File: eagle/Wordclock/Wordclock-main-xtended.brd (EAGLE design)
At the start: 100 x 50 mm, 59 parts, among them IC1 MEGA8-P, J1 AVR_SPI_PRG_6PTH, Q1 16MHz, T1 EBC pinout

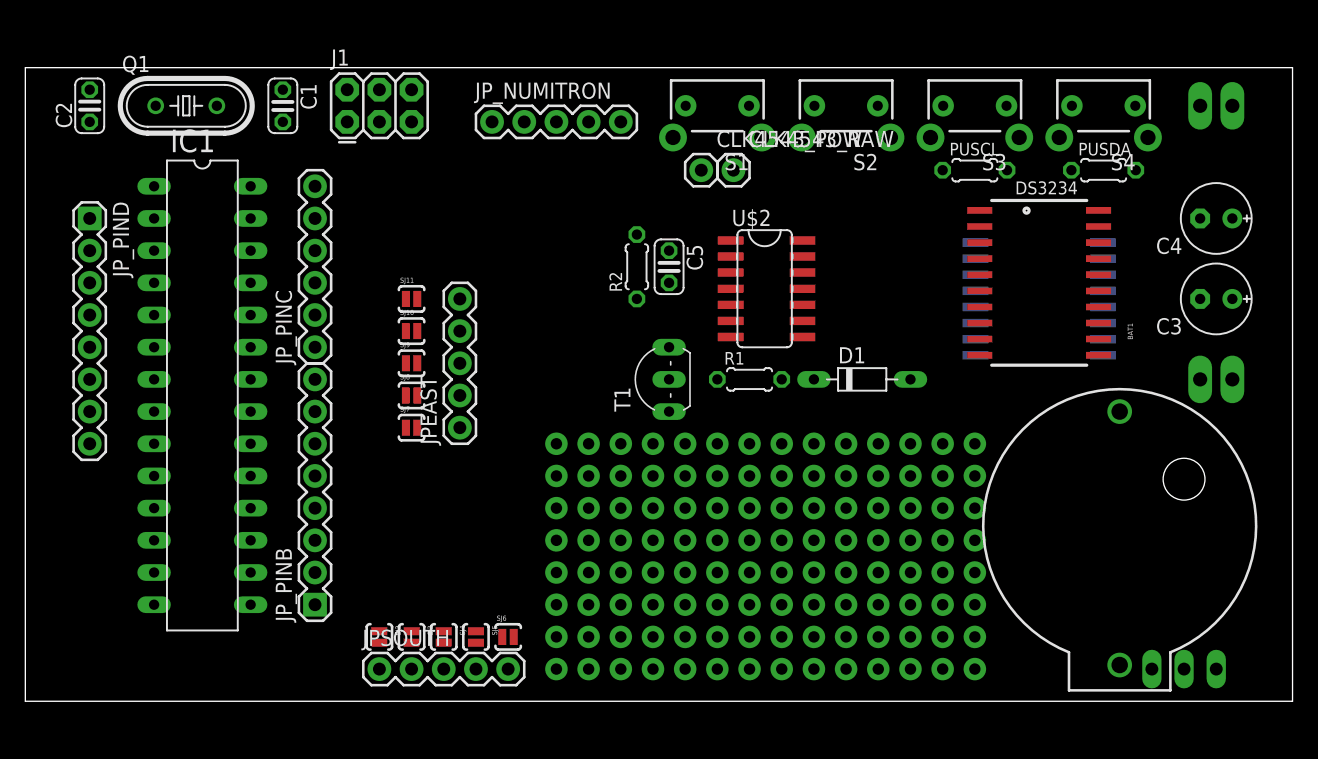
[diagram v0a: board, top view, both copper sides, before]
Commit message: Worclock extended version wired beta, wired. Todo verify before production.
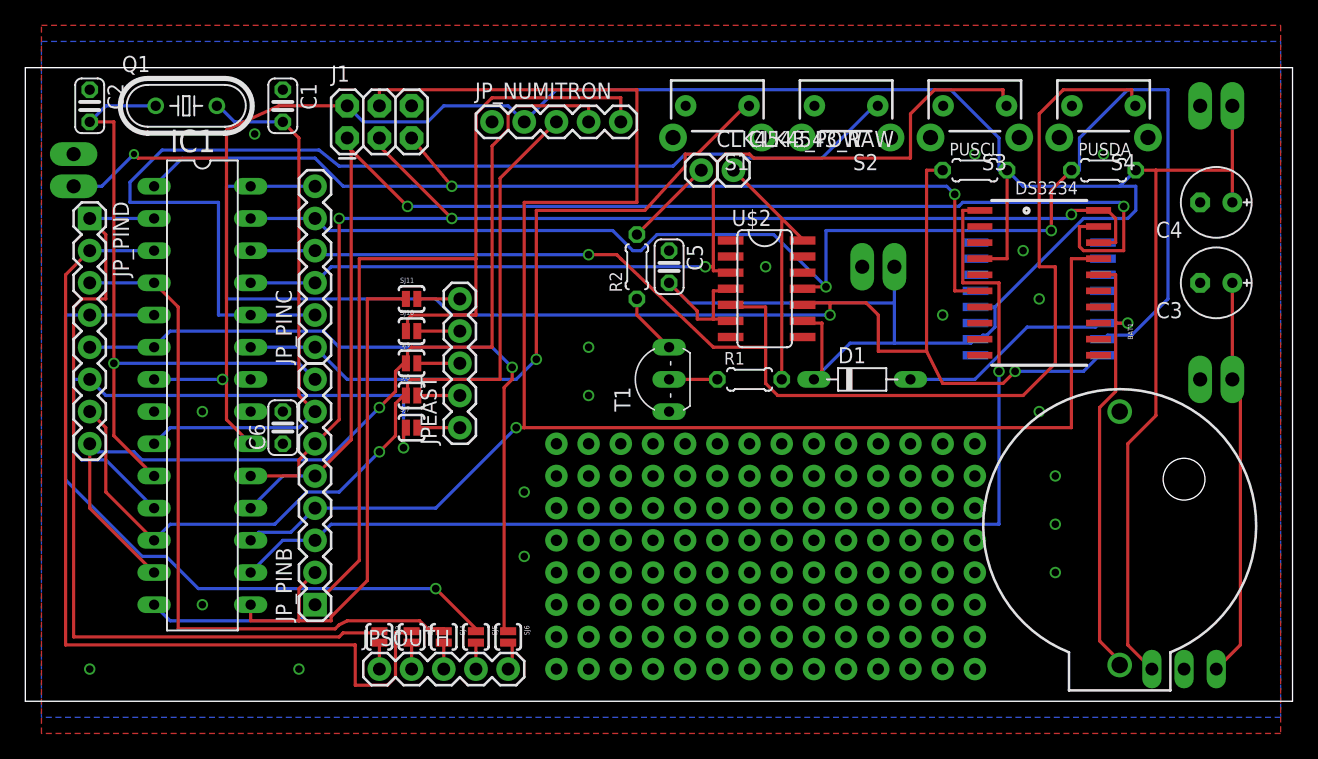
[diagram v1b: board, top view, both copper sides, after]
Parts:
- added C6: 1uF, resistor:C025-024X044
- added JP10, JP2: (no value), SparkFun-Connectors:1X02_LONGPADS
- moved C3 1.27 mm to (94.0, 33.0)
- moved C4 1.27 mm to (94.0, 39.4)
- moved J1 1.27 mm to (25.4, 44.5)
- turned C2 to 270 degrees
- turned SJ6 to 270 degrees
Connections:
- net GND: now also C6.2, JP10.1, JP2.1
- net VCC: now also C6.1, JP10.2, JP2.2
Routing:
- net VCC: track 0.00 -> 267.4 mm, vias 0 -> 2
- net N$14: track 0.00 -> 141.1 mm, vias 0 -> 1
- net N$31: track 0.00 -> 112.9 mm, vias 0 -> 2
- net N$30: track 0.00 -> 110.0 mm, vias 0 -> 2
- net N$32: track 0.00 -> 107.5 mm, vias 0 -> 1
- net N$13: track 0.00 -> 107.4 mm, vias 0 -> 2
- net N$12: track 0.00 -> 99.4 mm, vias 0 -> 3
- net N$6: track 0.00 -> 89.6 mm, vias 0 -> 1
- net N$26: track 0.00 -> 88.1 mm
- net N$2: track 0.00 -> 87.8 mm
- net RESET: track 0.00 -> 79.8 mm, vias 0 -> 2
- net N$27: track 0.00 -> 76.5 mm, vias 0 -> 1
- net N$7: track 0.00 -> 76.0 mm, vias 0 -> 1
- net N$21: track 0.00 -> 71.4 mm
- net N$28: track 0.00 -> 69.0 mm, vias 0 -> 1
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- added copper zone on layer 1, net GND
- added copper zone on layer 16, net GND

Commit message: Started adding the labels
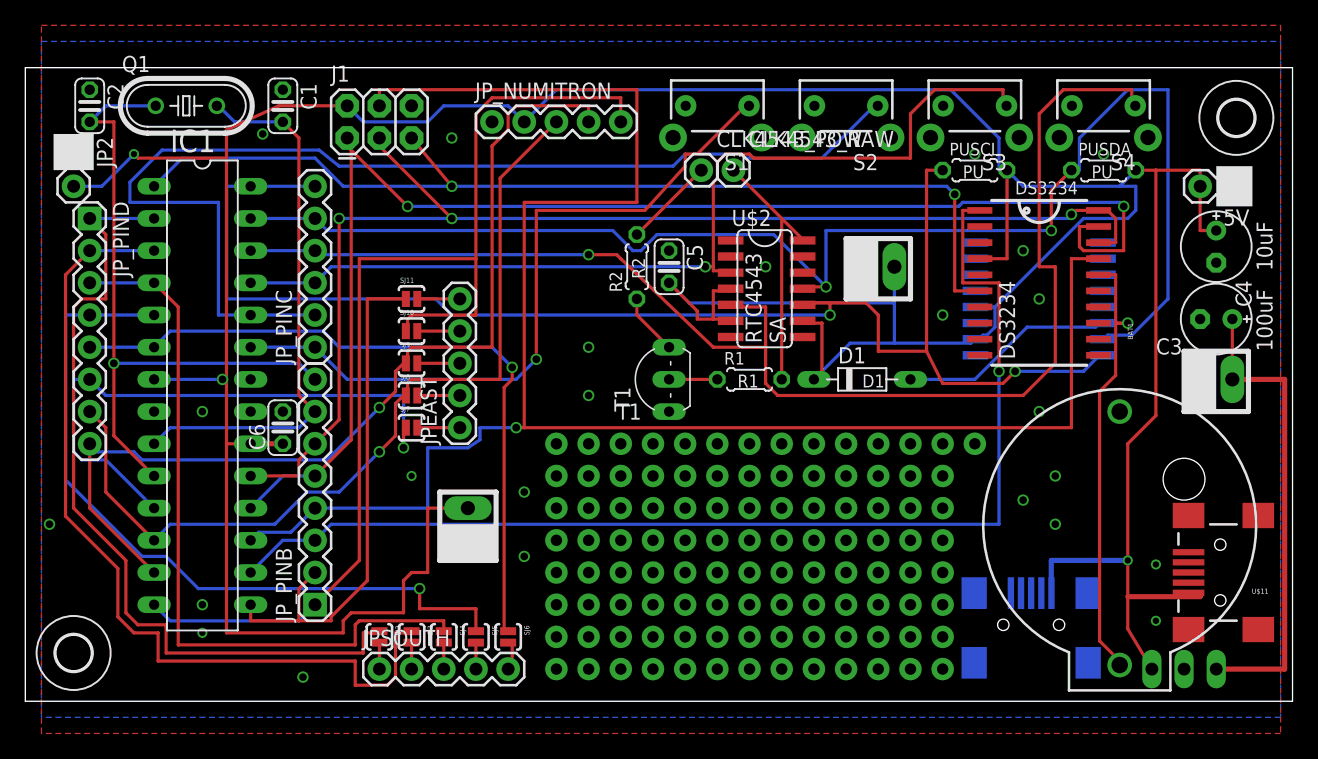
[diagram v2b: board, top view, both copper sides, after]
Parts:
- removed U$7: M7_NOSILK, kalshagar:M7_NOSILK
- added H1, H2: MOUNT-HOLE2.8, holes:2,8
- added JP11: (no value), SparkFun-Connectors:1X02_LONGPADS
- added U$11, U$12: USB-MINIB-5PIN, SparkFun-Connectors:USB-MINIB
- 5V: device SparkFun:1X02_LONGPADS -> SparkFun-Connectors:1X02
- JP2: device SparkFun-Connectors:1X02_LONGPADS -> SparkFun-Connectors:1X02
- moved 5V 6.84 mm to (95.2, 40.6), turned to 180 degrees
- moved C4 3.49 mm to (94.0, 35.9), turned to 270 degrees
- moved C3 2.86 mm to (94.0, 30.2)
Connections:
- net GND: now also JP11.1, U$11.GND, U$12.GND
- net VCC: now also JP11.2, U$11.VBUS, U$12.VBUS
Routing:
- net VCC: track 267.4 -> 325.1 mm, vias 2 -> 3
- net VIN: track 31.5 -> 37.1 mm
- net N$14: track 141.1 -> 144.4 mm
- net N$21: track 71.4 -> 68.2 mm
- net N$22: track 54.8 -> 57.9 mm
- net N$23: track 57.4 -> 59.3 mm
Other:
- board text added: "100uF"
- board text added: "10uF"
- board text added: "D1"
- board text added: "DS3231"
- board text added: "DS3234"
- board text added: "PU"
- board text added: "R1"
- board text added: "R2"
- board text added: "RTC4543"
- board text added: "SA"
- board text added: "T1"

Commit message: Added labels, need a final review and go to production.
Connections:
- net GND: now also U$8.P$1, U$8.P$2, U$8.P$3, U$8.P$4
- net VCC: now also U$10.P$1, U$8.P$5, U$8.P$6, U$8.P$7
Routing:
- net VCC: track 325.1 -> 339.7 mm
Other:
- board text added: "A"
- board text added: "ATmega-xx8"
- board text added: "B"
- board text added: "B0"
- board text added: "C"
- board text added: "C0"
- board text added: "C1"
- board text added: "CLK"
- board text added: "D"
- board text added: "D0"
- board text added: "DATA"
- board text added: "GND"
- board text added: "June2013"
- board text added: "LTCH"
- board text added: "Numitron"
- board text added: "RAW"
- board text added: "VCC"
- board text added: "Wordclock Xtended v1.0"
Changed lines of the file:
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@@
 <text x="48.895" y="33.3375" size="1.016" layer="21" rot="R90">R2</text>
 <text x="66.04" y="24.765" size="1.016" layer="21">D1</text>
+<text x="2.2225" y="39.0525" size="1.27" layer="21" rot="SR270">D0</text>
+<text x="25.7175" y="6.35" size="1.27" layer="21" rot="R90">B0</text>
+<text x="25.7175" y="26.9875" size="1.27" layer="21" rot="R90">C0</text>
+<wire x1="20.955" y1="26.67" x2="24.765" y2="26.67" width="0.254" layer="21"/>
+<text x="36.195" y="47.3075" size="1.27" layer="21">Numitron</text>
+<text x="37.465" y="40.3225" size="1.27" layer="21" rot="R90">GND</text>
+<text x="40.005" y="40.64" size="1.27" layer="21" rot="R90">VCC</text>
+<text x="42.545" y="40.64" size="1.27" layer="21" rot="R90">CLK</text>
+<text x="45.085" y="39.6875" size="1.27" layer="21" rot="R90">LTCH</text>
+<text x="47.625" y="39.6875" size="1.27" layer="21" rot="R90">DATA</text>
+<text x="13.335" y="32.385" size="1.27" layer="21" rot="R90">ATmega-xx8</text>
+<text x="6.6675" y="2.54" size="1.27" layer="21">Wordclock Xtended v1.0</text>
+<text x="10.795" y="0.9525" size="1.27" layer="21">June2013</text>
+<text x="51.435" y="36.83" size="1.27" layer="21" rot="R90">C1</text>
+<text x="54.2925" y="46.355" size="1.27" layer="21">A</text>
+<text x="64.4525" y="46.355" size="1.27" layer="21">B</text>
+<text x="74.295" y="46.355" size="1.27" layer="21">C</text>
+<text x="84.455" y="46.355" size="1.27" layer="21">D</text>
+<text x="98.425" y="22.86" size="1.27" layer="21" rot="R90">RAW</text>
+<wire x1="40.64" y1="21.59" x2="43.18" y2="21.59" width="0.254" layer="21"/>
+<wire x1="43.18" y1="21.59" x2="43.18" y2="11.43" width="0.254" layer="21"/>
+<wire x1="43.18" y1="11.43" x2="43.18" y2="1.27" width="0.254" layer="21"/>
+<wire x1="43.18" y1="1.27" x2="40.64" y2="1.27" width="0.254" layer="21"/>
+<wire x1="40.64" y1="1.27" x2="40.64" y2="11.43" width="0.254" layer="21"/>
+<wire x1="40.64" y1="11.43" x2="40.64" y2="21.59" width="0.254" layer="21"/>
+<wire x1="40.64" y1="11.43" x2="43.18" y2="11.43" width="0.254" layer="21"/>
+<text x="40.64" y="21.9075" size="1.016" layer="21">VCC</text>
+<text x="40.3225" y="0" size="1.016" layer="21">GND</text>
+<wire x1="35.56" y1="46.355" x2="35.56" y2="48.895" width="0.254" layer="21"/>
+<wire x1="35.56" y1="48.895" x2="48.26" y2="48.895" width="0.254" layer="21"/>
+<wire x1="48.26" y1="48.895" x2="48.26" y2="46.0375" width="0.254" layer="21"/>
 </plain>
 <attributes>
@@
 <via x="89.2175" y="6.35" extent="1-16" drill="0.5" shape="square"/>
 <contactref element="U$12" pad="GND"/>
+<via x="79.375" y="48.5775" extent="1-16" drill="0.5" shape="square"/>
+<contactref element="U$8" pad="P$1"/>
+<contactref element="U$8" pad="P$2"/>
+<contactref element="U$8" pad="P$3"/>
+<contactref element="U$8" pad="P$4"/>
 </signal>
 <signal name="N$30">
@@
 <via x="86.995" y="11.1125" extent="1-16" drill="0.5"/>
 <wire x1="92.71" y1="8.255" x2="91.7575" y2="8.5725" width="0.4064" layer="1"/>
+<contactref element="U$8" pad="P$5"/>
+<contactref element="U$8" pad="P$6"/>
+<contactref element="U$8" pad="P$7"/>
+<wire x1="41.91" y1="12.7" x2="41.91" y2="15.24" width="0.4064" layer="1"/>
+<wire x1="41.91" y1="15.24" x2="41.91" y2="17.78" width="0.4064" layer="1"/>
+<wire x1="34.925" y1="15.24" x2="41.91" y2="15.24" width="0.4064" layer="16"/>
+<contactref element="U$10" pad="P$1"/>
+<wire x1="41.91" y1="17.78" x2="41.91" y2="20.32" width="0.4064" layer="16"/>
 <wire x1="91.7575" y1="8.5725" x2="91.7975" y2="8.56" width="0" layer="19" extent="1-1"/>
 <wire x1="80.975" y1="8.5325" x2="80.9625" y2="8.5725" width="0" layer="19" extent="16-16"/>

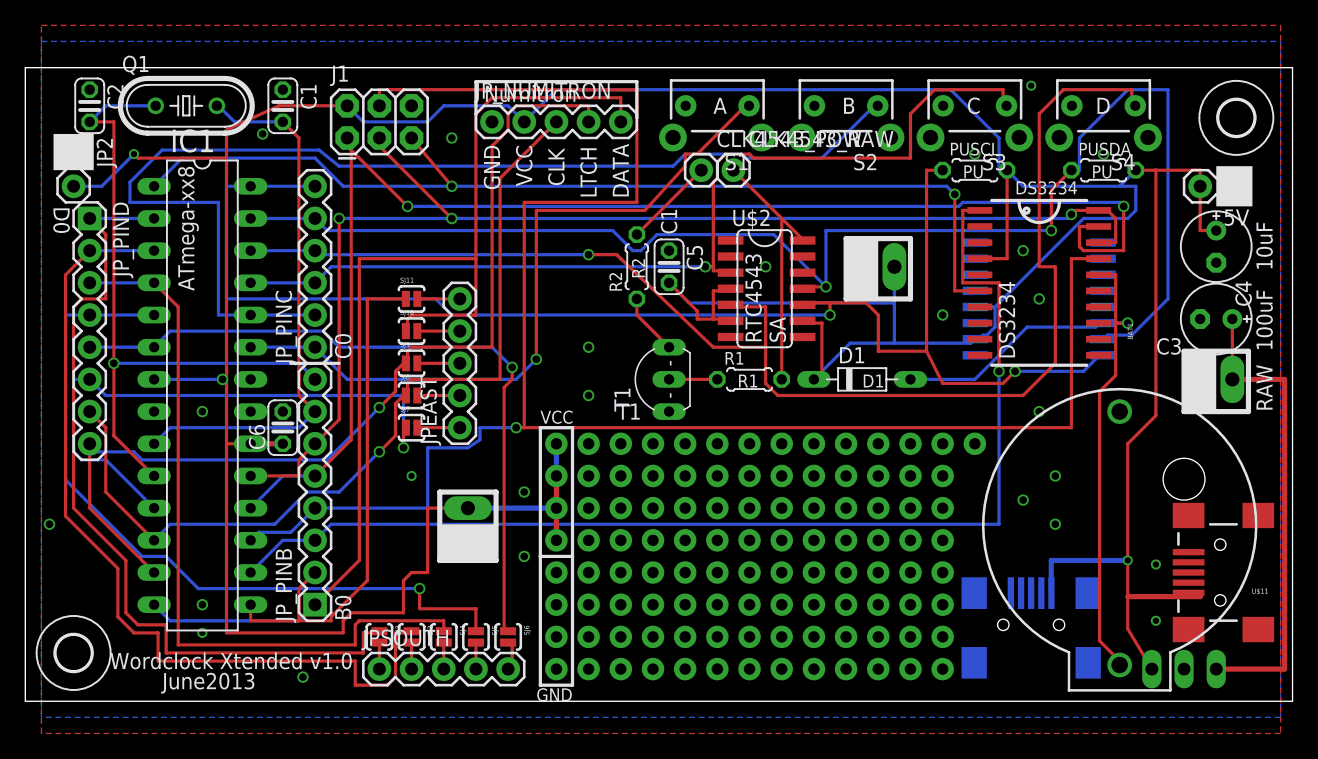
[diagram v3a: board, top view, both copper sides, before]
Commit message: Extended wordlock main board sent to production.
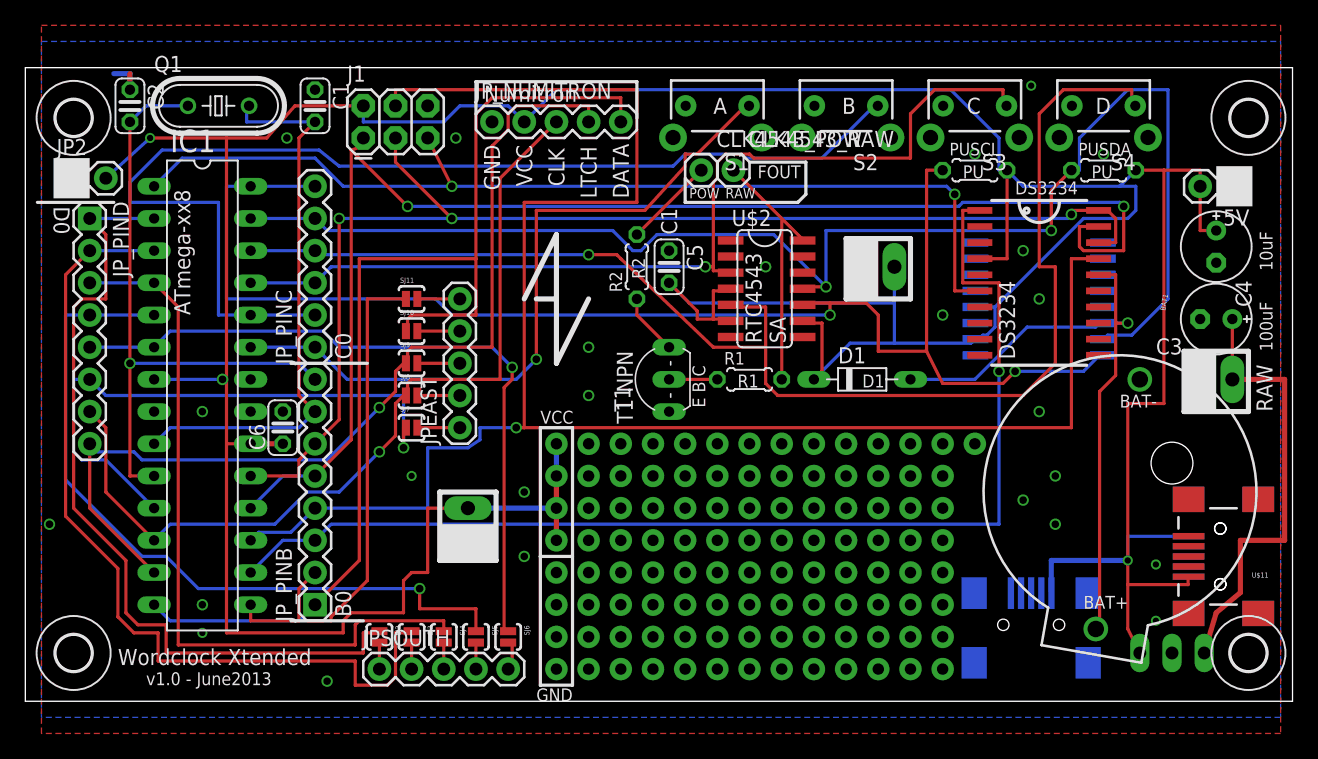
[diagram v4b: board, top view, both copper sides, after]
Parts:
- added H3, H4: MOUNT-HOLE2.8, holes:2,8
- added U$7: USB-MINIB-5PIN, SparkFun-Connectors:USB-MINIB
- moved C2 3.18 mm to (8.26, 47.0)
- moved BAT1 3.00 mm to (87.9, 25.4), turned to 260 degrees
- moved Q1 2.54 mm to (15.2, 47.0)
- moved C1 2.54 mm to (22.9, 47.0)
- moved JP2 1.91 mm to (3.81, 41.3), turned to 0 degrees
- moved IC2 1.59 mm to (90.5, 7.62)
- moved J1 1.27 mm to (26.7, 44.5)
- moved U$11 1.27 mm to (94.3, 11.4)
- moved H2 0.95 mm to (96.5, 46.0)
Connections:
- net GND: now also U$7.GND
- net VCC: now also U$7.VBUS
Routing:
- net VCC: track 339.7 -> 343.7 mm
- net GND: track 0.00 -> 3.81 mm
- net BATP: track 53.3 -> 49.9 mm
- net N$5: track 53.3 -> 50.1 mm
- net VIN: track 37.1 -> 35.0 mm
- net N$14: track 144.4 -> 143.1 mm
- net N$4: track 43.4 -> 44.5 mm
- net RESET: track 79.8 -> 79.1 mm
- net N$13: track 107.4 -> 108.0 mm
- net N$12: track 99.4 -> 98.9 mm
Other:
- board text added: "BAT+"
- board text added: "BAT-"
- board text added: "E B C"
- board text added: "FOUT"
- board text added: "POW"
- board text added: "T1 NPN"
- board text added: "Wordclock Xtended"
- board text added: "http://kalshagar.wikispaces.com/WordClock"
- board text added: "v1.0 - June2013"
- board text removed: "June2013"
- board text removed: "T1"
- board text removed: "Wordclock Xtended v1.0"
